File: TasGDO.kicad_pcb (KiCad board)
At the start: 2 copper layers, 46 x 44 mm, 39 parts, among them J2 Conn_01x04_Pin, J3 Screw_Terminal_01x02, J4 Screw_Terminal_01x02, J6 Screw_Terminal_01x03, Q1 2N7002, Q2 2N7002, SW1 SW_Push, SW2 SW_Push, U1 ESP32-S3-MINI-2U, U2 TPS56339DDCR

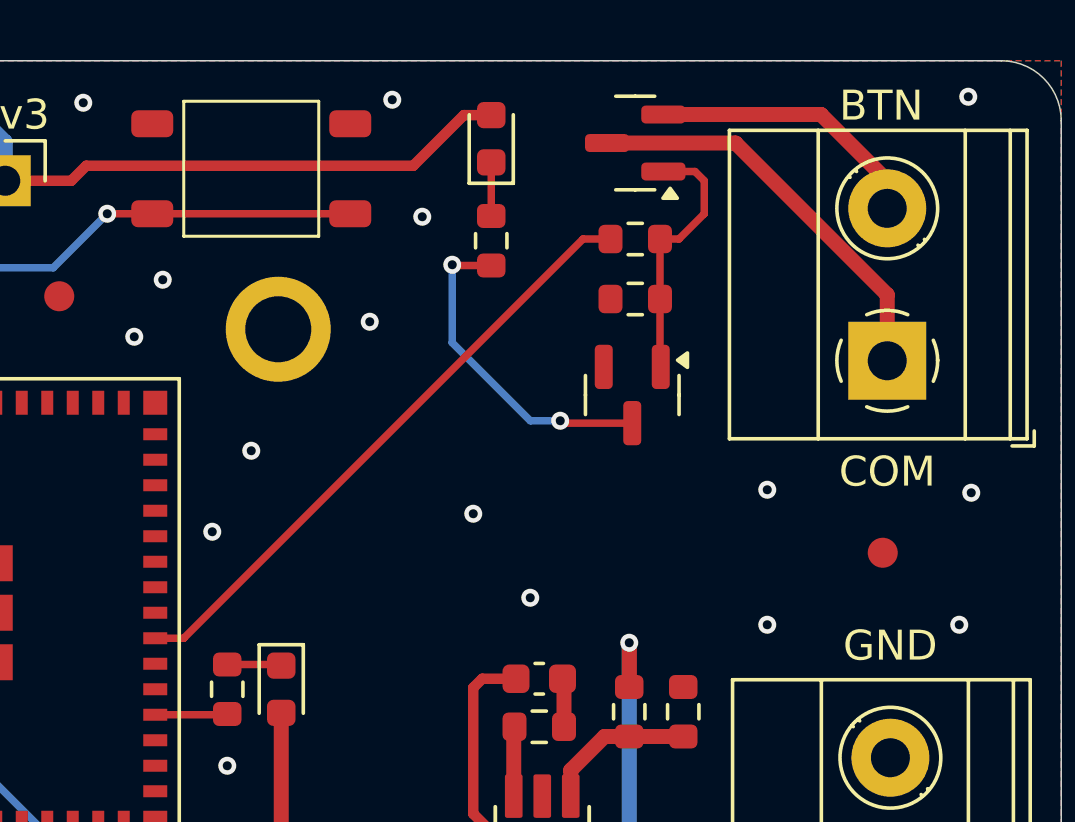
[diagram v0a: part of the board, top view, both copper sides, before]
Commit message: feat: switch to SSR
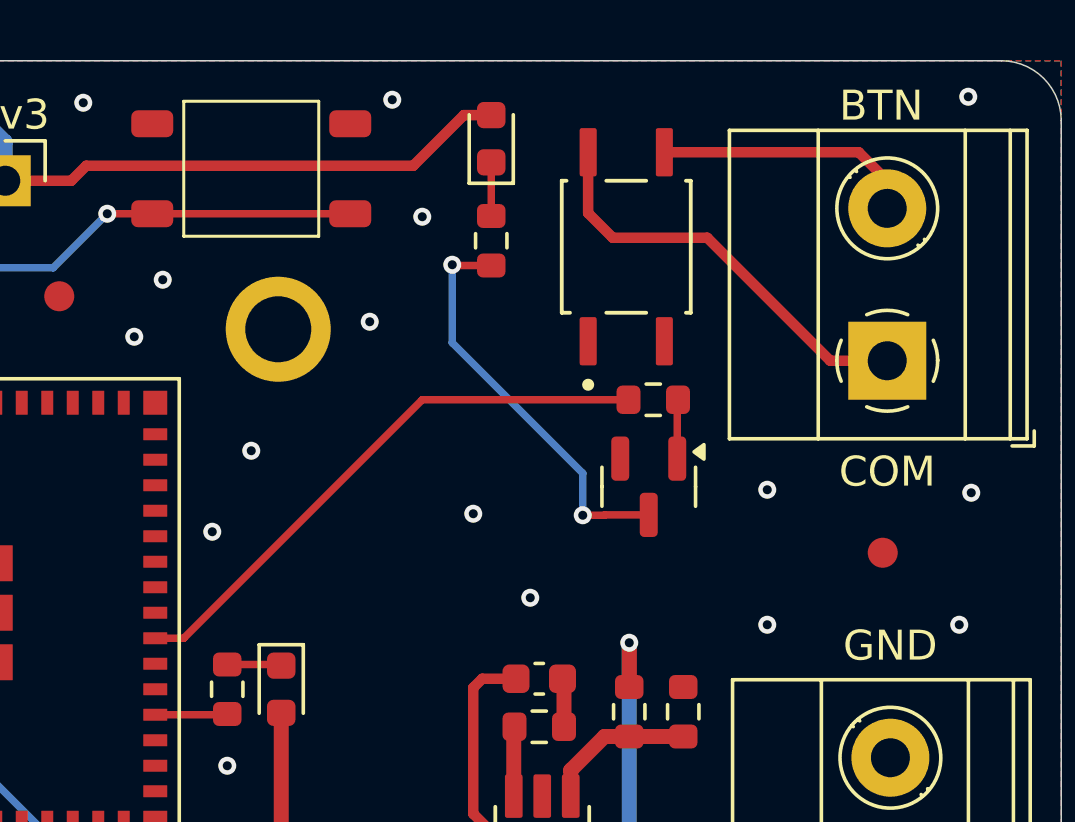
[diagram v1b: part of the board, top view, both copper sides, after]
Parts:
- removed Q1: 2N7002, Package_TO_SOT_SMD:SOT-23
- removed R3: 10K, Resistor_SMD:R_0603_1608Metric
- added K1: AQY212GSX, tasgdo:SOIC254P680X230-4N, F.Cu at (155.5, 75.2)
- R2: value 1K -> 330
- moved R2 5.39 mm to (156.4, 80.3)
- moved Q2 3.11 mm to (156.2, 83.2)
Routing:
- net /RELAY_LED: track 8.69 -> 1.97 mm
- net Net-(Q2-D): track 11.0 -> 13.7 mm
- net /RELAY: track 20.7 -> 19.1 mm
- net Net-(J3-Pin_2): track 9.30 -> 8.74 mm

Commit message: feat: minor changes
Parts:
- removed Q2: 2N7002, Package_TO_SOT_SMD:SOT-23
- D2: value YG -> B
- R2: value 330 -> 220
- moved R4 13.5 mm to (131.1, 97.5), turned to 90 degrees
- moved D2 13.4 mm to (133.6, 98.4), turned to 0 degrees
- moved R2 2.08 mm to (154.6, 81.3)
- moved U1 0.10 mm to (132.8, 87.5)
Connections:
- K1 pad 1: GND -> Net-(K1-Pad1)
- K1 pad 2: /RELAY_LED -> GND
- R2 pad 2: /RELAY_LED -> Net-(K1-Pad1)
- R5 pad 2: Net-(Q2-D) -> /RELAY_LED
- U1 pad 19: /ACT_LED -> unconnected-(U1-IO15-Pad19)
- U1 pad 21: unconnected-(U1-IO17-Pad21) -> /RELAY
- U1 pad 22: /RELAY -> /RELAY_LED
- U1 pad 6: unconnected-(U1-IO2-Pad6) -> /ACT_LED
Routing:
- net /RELAY_LED: track 1.97 -> 17.6 mm
- net Net-(Q2-D): track 13.7 -> 0.00 mm, vias 2 -> 0
- net +3.3V: track 127.2 -> 118.1 mm
- net Net-(K1-Pad1): track 0.00 -> 3.89 mm
- net /RELAY: track 19.1 -> 17.2 mm
- net GND: vias 34 -> 33

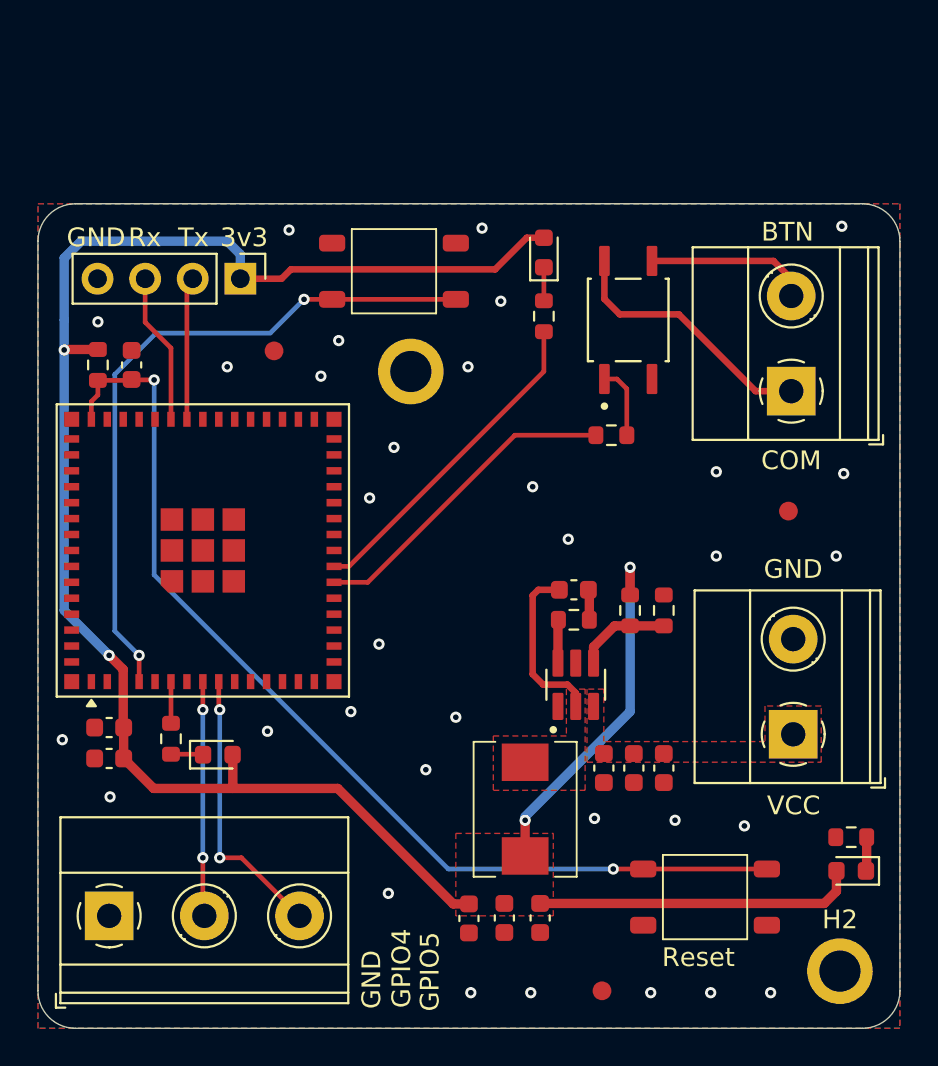
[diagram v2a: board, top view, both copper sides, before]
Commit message: feat: switch ESP32 ship
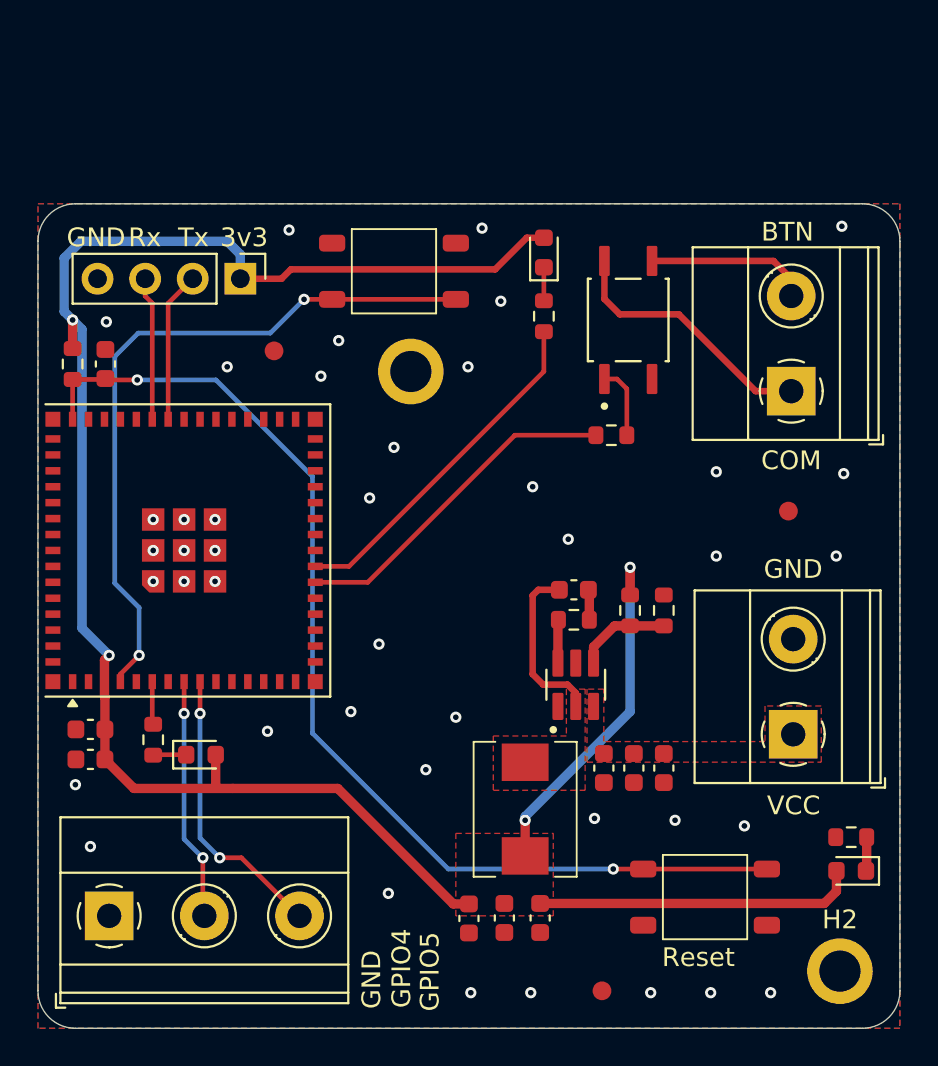
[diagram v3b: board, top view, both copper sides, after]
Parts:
- U1: footprint RF_Module:ESP32-S2-MINI-1U -> tasgdo:ESP32-S2-MINI-1
- moved U1 3.55 mm to (129.2, 87.5)
- moved C1 1.40 mm to (127.6, 77.5)
- moved R1 1.35 mm to (125.8, 77.5)
- moved C3 1.00 mm to (126.8, 97.0)
- moved C4 1.00 mm to (126.8, 98.7)
- moved R4 0.95 mm to (130.2, 97.6)
- moved D2 0.90 mm to (132.7, 98.4)
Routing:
- net /EN: track 54.8 -> 58.1 mm
- net /RELAY_LED: track 17.6 -> 18.6 mm
- net /RELAY: track 17.2 -> 18.2 mm
- net /BOOT_OPT: track 36.8 -> 37.8 mm
- net GND: vias 33 -> 42

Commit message: chore: bump to v0.2 (#5)
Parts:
- U1: value ESP32-S3-MINI-2U -> ESP32-S3-MINI-2
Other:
- board text added: "v0.2"
- board text removed: "v0.1"

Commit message: feat: miniaturise (#7)
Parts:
- removed C10, C8: 22u, Capacitor_SMD:C_0603_1608Metric
- removed C5: 10u, Capacitor_SMD:C_0603_1608Metric
- removed C7: 100n, Capacitor_SMD:C_0603_1608Metric
- removed D2: B, LED_SMD:LED_0603_1608Metric
- removed D3: Red, LED_SMD:LED_0603_1608Metric
- removed FID1, FID2, FID3: Fiducial, Fiducial:Fiducial_1mm_Mask2mm
- removed G***: LOGO, tasgdo:Logo
- removed H1, H2: MountingHole, MountingHole:MountingHole_2.2mm_M2_ISO7380_Pad
- removed J2: Conn_01x04_Pin, Connector_PinHeader_2.54mm:PinHeader_1x04_P2.54mm_Vertical
- removed J4: Screw_Terminal_01x02, TerminalBlock_Phoenix:TerminalBlock_Phoenix_MKDS-1,5-2-5.08_1x02_P5.08mm_Horizontal
- removed J6: Screw_Terminal_01x03, TerminalBlock_Phoenix:TerminalBlock_Phoenix_MKDS-1,5-3-5.08_1x03_P5.08mm_Horizontal
- removed R9: 10K, Resistor_SMD:R_0603_1608Metric
- removed U1: ESP32-S3-MINI-2, tasgdo:ESP32-S2-MINI-1
- added AE1: Ant_RFECA3216060A1T_1206, Hardware Components:Ant_RFECA3216060A1T, F.Cu at (144.4, 61.5)
- added C23: 12pF, Hardware Components:C_0402_1005Metric, F.Cu at (147.8, 68.2)
- added C24: 12pF, Hardware Components:C_0402_1005Metric, F.Cu at (147.4, 72.2)
- added C25: 2p7, Hardware Components:C_0402_1005Metric, F.Cu at (145.2, 66.8)
- added C26: 2p4, Hardware Components:C_0402_1005Metric, F.Cu at (146.6, 64.0)
- added C29: 100n, Hardware Components:C_0402_1005Metric, F.Cu at (138.6, 69.5)
- added C30: 100n, Hardware Components:C_0402_1005Metric, F.Cu at (140.8, 74.0)
- added C34: 1u, Hardware Components:C_0402_1005Metric, F.Cu at (147.8, 66.2)
- added D1: D_Schottky_Small, Hardware Components:D_0402_1005Metric, F.Cu at (150.4, 80.9)
- added D5: LED_Dual_AAKK, Hardware Components:LED_LiteOn_LTST-C295K_1.6x0.8mm, F.Cu at (134.6, 70.2)
- added J1: Conn_01x04, Hardware Components:Conn_JST_PH_S4B-PH-K_1x04_P2.00mm_Horizontal, F.Cu at (137.0, 73.7)
- added J10: USB_C_Receptacle_USB2.0_16P, Hardware Components:USB_C_Receptacle_HRO_TYPE-C-31-M-12, F.Cu at (144.3, 80.2)
- added R13: 5k1, Hardware Components:R_0402_1005Metric, F.Cu at (142.8, 74.3)
- added R14: 5k1, Hardware Components:R_0402_1005Metric, F.Cu at (146.9, 74.3)
- added R3: 10k, Hardware Components:R_0402_1005Metric, F.Cu at (139.3, 67.0)
- added U3: ESP32-C3, Hardware Components:QFN-32-1EP, F.Cu at (142.6, 70.4)
- added Y2: ECS-400-10-37B2-CKM-TR, Hardware Components:Oscillator_ECS_400-10-37B2-CKM-TR, F.Cu at (147.4, 70.2)
- C1, C3, C4: footprint Capacitor_SMD:C_0603_1608Metric -> Hardware Components:C_0402_1005Metric
- C2: value 100n -> 10n; footprint Capacitor_SMD:C_0603_1608Metric -> Hardware Components:C_0402_1005Metric
- C6: footprint Capacitor_SMD:C_0603_1608Metric -> Hardware Components:C_0805_2012Metric
- C9: value 100n -> 10u; footprint Capacitor_SMD:C_0603_1608Metric -> Hardware Components:C_0805_2012Metric
- D4: footprint LED_SMD:LED_0603_1608Metric -> Hardware Components:LED_0603_1608Metric
- J3: value Screw_Terminal_01x02 -> Conn_01x03; footprint TerminalBlock_Phoenix:TerminalBlock_Phoenix_MKDS-1,5-2-5.08_1x02_P5.08mm_Horizontal -> Hardware Components:Conn_JST_PH_S3B-PH-K_1x03_P2.00mm_Horizontal
- K1: footprint tasgdo:SOIC254P680X230-4N -> Hardware Components:SSR_SUPSiC_GAQY212GSX
- L1: value 4.7uH -> 2.4nH; footprint tasgdo:YSPI0530 -> Hardware Components:L_0402_1005Metric
- R1, R2, R4, R5, R6: footprint Resistor_SMD:R_0603_1608Metric -> Hardware Components:R_0402_1005Metric
- R7: value 30 -> 10k; footprint Resistor_SMD:R_0603_1608Metric -> Hardware Components:R_0402_1005Metric
- R8: value 30.9K -> 10k; footprint Resistor_SMD:R_0603_1608Metric -> Hardware Components:R_0402_1005Metric
- SW1: footprint tasgdo:K2-1109SP-B4SA-01 -> Hardware Components:SW_PTS815SJM250SMTRLFS
- SW2: value SW_Push -> KSC241J LFS; footprint tasgdo:K2-1109SP-B4SA-01 -> Hardware Components:SW_CK_KSC241JLFS; moved to B.Cu
- U2: value TPS56339DDCR -> Conv_AMS1117S-3.3; footprint tasgdo:TPS56339DDCR -> Hardware Components:SOT-89-3
- moved SW1 44.3 mm to (152.2, 62.3), turned to 0 degrees
- moved R6 37.6 mm to (154.2, 67.7)
- moved D4 37.1 mm to (154.3, 69.9), turned to -90 degrees
- moved C4 36.9 mm to (141.1, 64.6), turned to 90 degrees
- moved L1 36.2 mm to (145.8, 65.4), turned to 45 degrees
- moved C3 35.4 mm to (142.6, 65.4), turned to 45 degrees
- moved C9 34.1 mm to (154.3, 73.2), turned to -90 degrees
- moved J3 31.8 mm to (137.0, 62.6), turned to -90 degrees
- moved R1 31.1 mm to (154.2, 64.7), turned to 180 degrees
- moved R4 28.7 mm to (136.7, 69.7), turned to 0 degrees
- moved C1 27.8 mm to (152.3, 64.7), turned to 180 degrees
- moved R7 24.9 mm to (138.5, 70.7)
- moved R8 23.7 mm to (139.3, 73.5)
- moved C2 22.9 mm to (147.8, 67.2), turned to 0 degrees
- moved C6 18.8 mm to (152.7, 81.0), turned to 180 degrees
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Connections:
- net Net-(J4-Pin_1) renamed VCC
- C2 pad 1: Net-(C2-Pad1) -> +3.3V
- C2 pad 2: Net-(U2-SW) -> GND
- J3 pad 1: Net-(J3-Pin_1) -> GND
- J3 pad 2: Net-(J3-Pin_2) -> /GPIO4
- K1 pad 3: Net-(J3-Pin_2) -> /COM
- K1 pad 4: Net-(J3-Pin_1) -> /BTN
- L1 pad 1: Net-(U2-SW) -> /RF_ANT
- L1 pad 2: +3.3V -> /RF_FEED
- R7 pad 1: Net-(U2-BOOT) -> +3.3V
- R7 pad 2: Net-(C2-Pad1) -> Net-(U3-GPIO8)
- R8 pad 1: Net-(U2-FB) -> +3.3V
- R8 pad 2: +3.3V -> /BOOT_OPT
- U2 pad 2: Net-(U2-SW) -> +3.3V
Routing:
- net +3.3V: track 118.6 -> 13.2 mm, vias 4 -> 14
- net /EN: track 58.1 -> 22.2 mm
- net /BOOT_OPT: track 37.8 -> 10.7 mm, vias 2 -> 1
- net /VBUS: track 0.00 -> 16.2 mm, vias 0 -> 3
- net /BTN: track 0.00 -> 16.1 mm, vias 0 -> 1
- net /COM: track 0.00 -> 15.5 mm, vias 0 -> 1
- net /RELAY_LED: track 18.6 -> 3.27 mm
- net VCC: track 0.00 -> 14.2 mm
- net Net-(J3-Pin_1): track 14.0 -> 0.00 mm
- net /GPIO5: track 15.4 -> 4.21 mm, vias 2 -> 0
- net Net-(U2-SW): track 9.19 -> 0.00 mm
- net Net-(J3-Pin_2): track 8.74 -> 0.00 mm
- net /USB_P: track 0.00 -> 8.63 mm
- net /USB_N: track 0.00 -> 8.59 mm
- net /TX: track 8.04 -> 0.00 mm
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- added copper zone on In2.Cu, net +3.3V
- added copper zone on In1.Cu, net GND
- removed copper zone on F.Cu, net Net-(U2-SW)
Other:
- board size 46 x 44 mm -> 22 x 22.2 mm
- copper layers 2 -> 4
- board text added: "0"
- board text added: "0 mm"
- board text added: "0.01 mm"
- board text added: "0.0152 mm"
- board text added: "0.02"
- board text added: "0.035 mm"
- board text added: "0.127 mm / 0.15 mm"
- board text added: "0.2000 mm"
- board text added: "0.2104 mm"
- board text added: "1"
- board text added: "1.065 mm"
- board text added: "1.6062 mm"
- board text added: "22 mm x 22 mm"
- board text added: "3.3"
- board text added: "4"
- board text added: "4.4"
- board text added: "4.6"
- board text added: "7628"
- board text added: "B.Cu"
- board text added: "B.Mask"
- board text added: "B.Paste"
- board text added: "B.Silkscreen"
- board text added: "BOARD CHARACTERISTICS"
- board text added: "Black"
- board text added: "Board Thickness:"
- board text added: "Board overall dimensions:"
- board text added: "Bottom Silk Screen"
- board text added: "Bottom Solder Mask"
- board text added: "Bottom Solder Paste"
- board text added: "Castellated pads:"
- board text added: "Color"
- board text added: "Copper Finish:"
- board text added: "Copper Layer Count:"
- board text added: "Dielectric 1"
- board text added: "Dielectric 2"
- board text added: "Dielectric 3"
- board text added: "Edge card connectors:"
- board text added: "Epsilon R"
- board text added: "F.Cu"
- board text added: "F.Mask"
- board text added: "F.Paste"
- board text added: "F.Silkscreen"
- board text added: "FR4"
- board text added: "HASL"
- board text added: "Impedance Control:"
- board text added: "Impedance control"
- board text added: "In1.Cu"
- board text added: "In2.Cu"
- board text added: "Layer Name"
- board text added: "Loss Tangent"
- board text added: "Material"
- board text added: "Min hole diameter:"
- board text added: "Min track/spacing:"
- board text added: "No"
- board text added: "Plated Board Edge:"
- board text added: "RST"
- board text added: "Thickness (mm)"
- board text added: "Top Silk Screen"
- board text added: "Top Solder Mask"
- board text added: "Top Solder Paste"
- board text added: "Type"
- board text added: "White"
- board text added: "Yes"
- board text added: "copper"
- board text added: "core"
- board text added: "prepreg"
- board text added: "v0.3"
- board text removed: "3v3"
- board text removed: "BTN"
- board text removed: "COM"
- board text removed: "GND"
- board text removed: "GPIO4"
- board text removed: "GPIO5"
- board text removed: "Reset"
- board text removed: "Rx"
- board text removed: "Tx"
- board text removed: "VCC"
- board text removed: "v0.2"

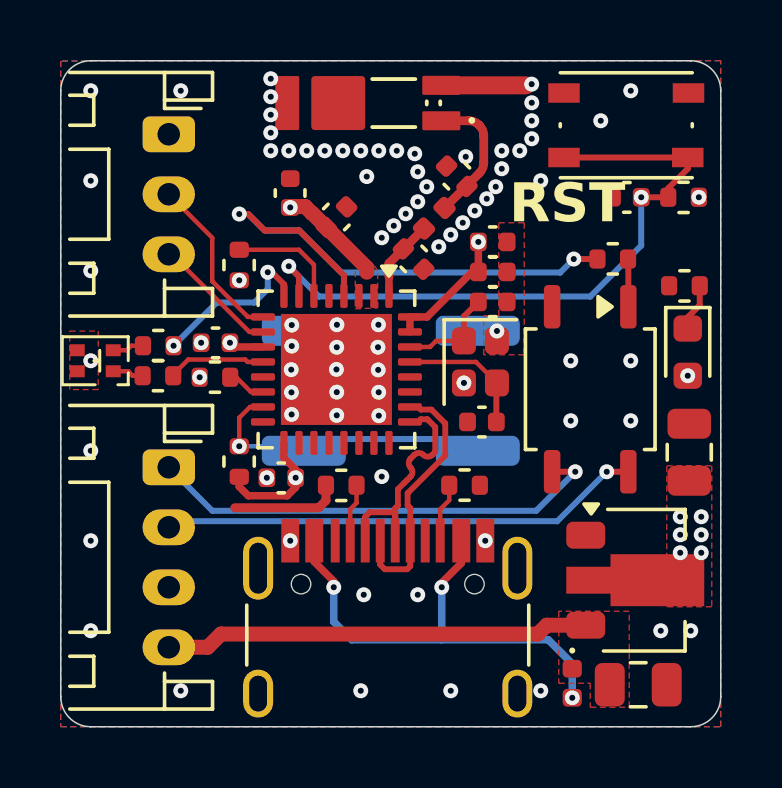
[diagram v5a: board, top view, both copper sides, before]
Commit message: fix: replace LDO to switching supply (#8)
* fix: switch to switching power supply

* chore: update board image

* chore: add readme header

* feat: update production files
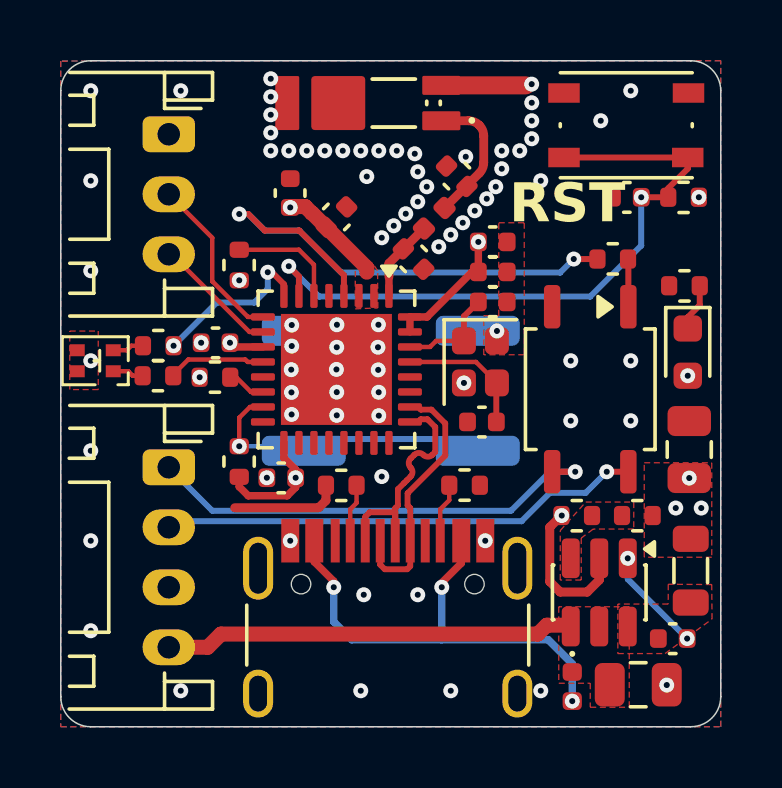
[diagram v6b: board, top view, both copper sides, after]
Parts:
- removed U2: Conv_AMS1117S-3.3, Hardware Components:SOT-89-3
- added C5: 100n, Hardware Components:C_0402_1005Metric, F.Cu at (153.8, 79.4)
- added L2: 10u, Hardware Components:L_0805_2012Metric, F.Cu at (154.4, 77.1)
- added R10: 69k8, Hardware Components:R_0402_1005Metric, F.Cu at (152.6, 75.3)
- added R9: 22k1, Hardware Components:R_0402_1005Metric, F.Cu at (150.6, 75.3)
- added U1: Conv_LMR54410DBVR, Hardware Components:SOT-23-6, F.Cu at (151.3, 77.9)
- C9: value 10u -> 22u
- moved D1 0.11 mm to (150.4, 81.0)
- moved C9 0.09 mm to (154.3, 73.1)
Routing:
- net GND: track 6.47 -> 11.5 mm
- net Net-(U1-CB): track 0.00 -> 3.50 mm, vias 0 -> 2
- net +3.3V: vias 14 -> 11
- added copper zone on F.Cu, net Net-(U1-FB)
- added copper zone on F.Cu, net Net-(U1-SW)
